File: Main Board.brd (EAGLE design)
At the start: 82.5 x 69.8 mm, 4 parts

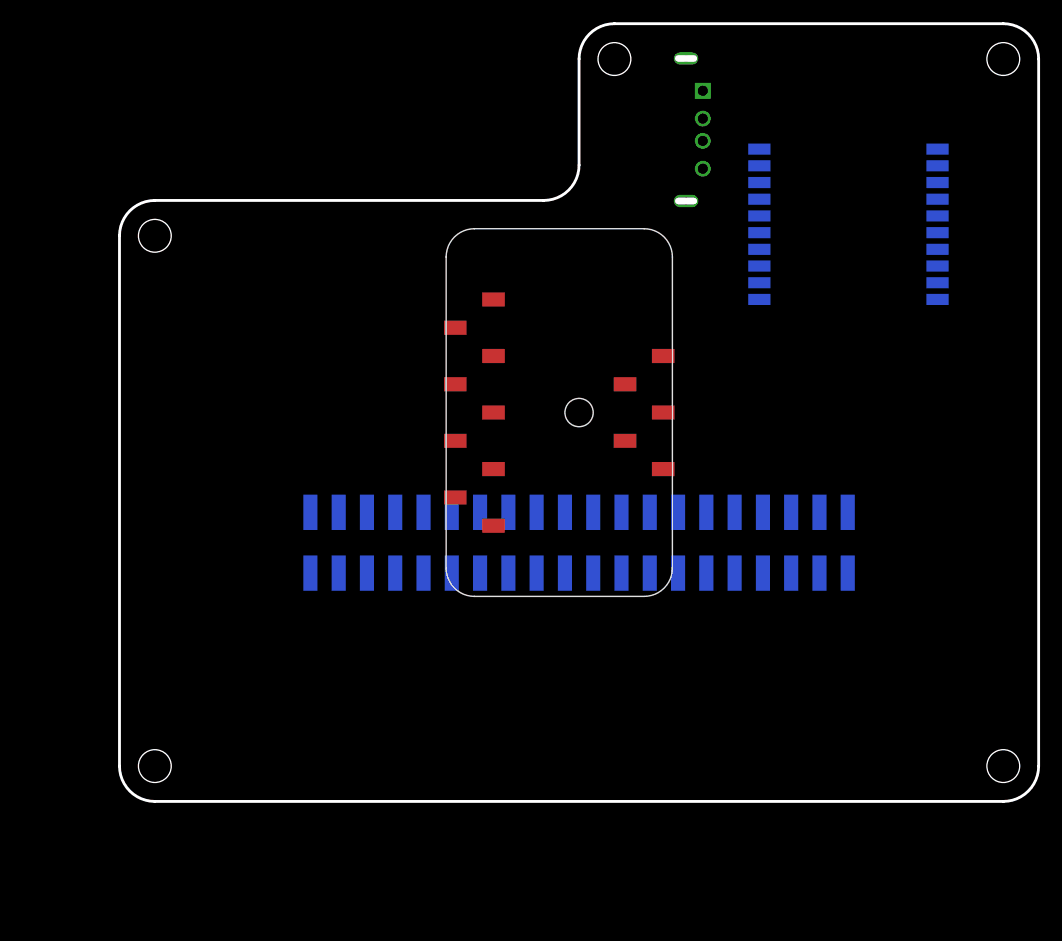
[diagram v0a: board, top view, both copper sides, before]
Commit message: Added Vishay and Bourns part libraries
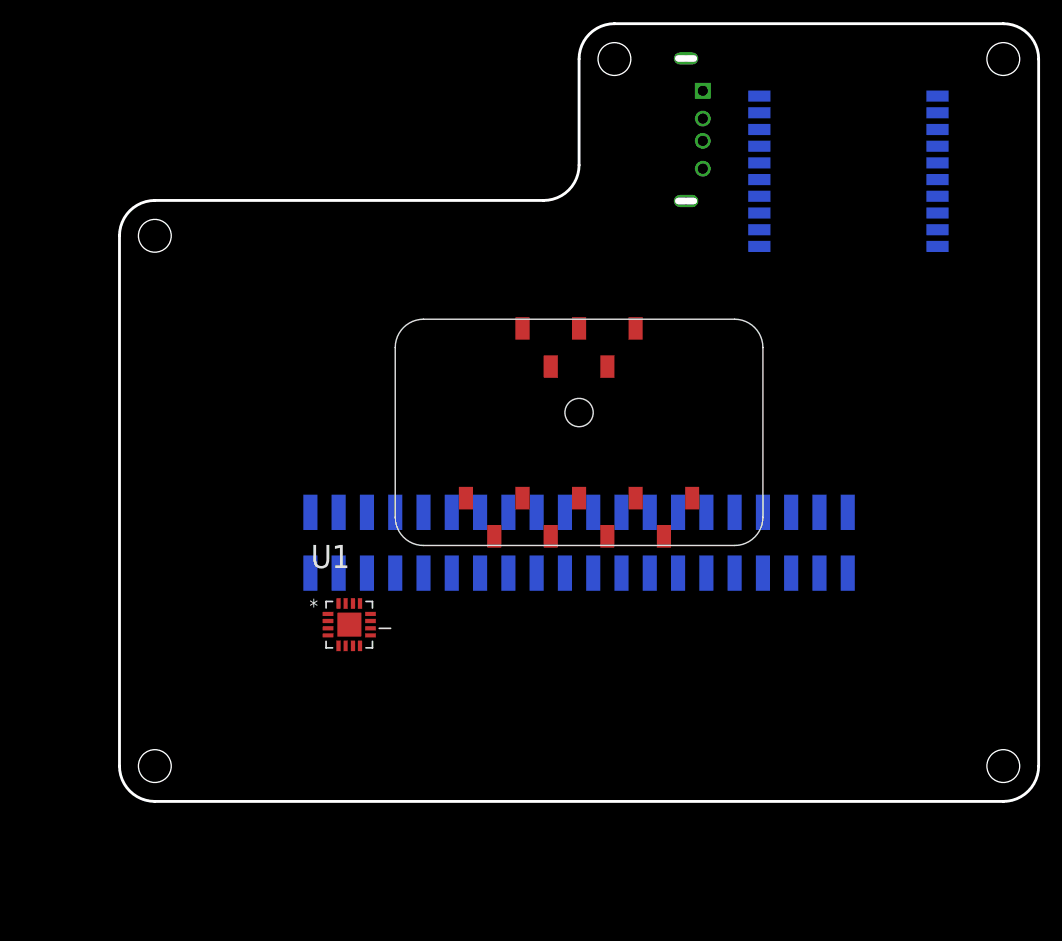
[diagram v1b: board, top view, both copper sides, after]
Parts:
- added U1: TPS61030RSAR, Texas Instruments:QFN65P400X400X100-17N
- moved U$5 4.76 mm to (23.8, 17.5)
- turned U$6 to 0 degrees
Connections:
- new net VBAT: U1.11, U1.8
- net +5V: now also U1.1, U1.15, U1.16
- net GND: now also U1.10, U1.13, U1.2, U1.5, U1.6, U1.7
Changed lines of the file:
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@@
 </autorouter>
 <elements>
-<element name="U$5" library="GoatFinder" package="GPS" value="GPS" x="23.8125" y="12.7" rot="MR180"/>
-<element name="U$6" library="GoatFinder" package="9DOF" value="9DOF" x="0" y="0" rot="R270"/>
+<element name="U$5" library="GoatFinder" package="GPS" value="GPS" x="23.8125" y="17.4625" rot="MR180"/>
+<element name="U$6" library="GoatFinder" package="9DOF" value="9DOF" x="0" y="0"/>
 <element name="U$8" library="GoatFinder" package="USB_VERTICLE" value="USB_VERTICLE" x="11.1125" y="25.4" rot="R90"/>
 <element name="U$11" library="GoatFinder" package="PI_HEADER_SMD" value="PI" x="0" y="-11.5"/>
+<element name="U1" library="Texas Instruments" package="QFN65P400X400X100-17N" value="TPS61030RSAR" x="-20.6375" y="-19.05">
+<attribute name="MPN" value="TPS61030RSAR" x="-20.6375" y="-19.05" size="1.778" layer="27" display="off"/>
+<attribute name="OC_FARNELL" value="1813710" x="-20.6375" y="-19.05" size="1.778" layer="27" display="off"/>
+<attribute name="OC_NEWARK" value="90H4859" x="-20.6375" y="-19.05" size="1.778" layer="27" display="off"/>
+<attribute name="PACKAGE" value="QFN-16" x="-20.6375" y="-19.05" size="1.778" layer="27" display="off"/>
+<attribute name="SUPPLIER" value="Texas Instruments" x="-20.6375" y="-19.05" size="1.778" layer="27" display="off"/>
+</element>
 </elements>
 <signals>
@@
 <contactref element="U$11" pad="5V@4"/>
 <contactref element="U$6" pad="P$20"/>
-<wire x1="-7.683" y1="10.16" x2="11.1125" y2="28.9" width="0" layer="19" extent="1-1"/>
-<wire x1="-21.59" y1="-14.421" x2="-7.683" y2="10.16" width="0" layer="19" extent="1-16"/>
+<contactref element="U1" pad="16"/>
+<contactref element="U1" pad="15"/>
+<contactref element="U1" pad="1"/>
+<wire x1="-10.16" y1="-7.683" x2="11.1125" y2="28.9" width="0" layer="19" extent="1-1"/>
+<wire x1="-21.59" y1="-14.421" x2="-10.16" y2="-7.683" width="0" layer="19" extent="1-16"/>
 <wire x1="-24.13" y1="-14.421" x2="-21.59" y2="-14.421" width="0" layer="19" extent="16-16"/>
+<wire x1="-21.6027" y1="-17.145" x2="-21.59" y2="-14.421" width="0" layer="19" extent="1-16"/>
+<wire x1="-20.9677" y1="-17.145" x2="-21.6027" y2="-17.145" width="0" layer="19" extent="1-1"/>
+<wire x1="-22.5425" y1="-18.0848" x2="-21.6027" y2="-17.145" width="0" layer="19" extent="1-1"/>
 </signal>
 <signal name="GND">
@@
 <contactref element="U$11" pad="GND@39"/>
 <contactref element="U$6" pad="P$22"/>
-<wire x1="32.1925" y1="11.66" x2="32.1925" y2="22.16" width="0" layer="19" extent="16-16"/>
-<wire x1="16.1925" y1="20.66" x2="32.1925" y2="22.16" width="0" layer="19" extent="16-16"/>
-<wire x1="11.1125" y1="21.9" x2="16.1925" y2="20.66" width="0" layer="19" extent="16-16"/>
+<contactref element="U1" pad="7"/>
+<contactref element="U1" pad="5"/>
+<contactref element="U1" pad="6"/>
+<contactref element="U1" pad="13"/>
+<contactref element="U1" pad="10"/>
+<contactref element="U1" pad="2"/>
+<wire x1="32.1925" y1="16.4225" x2="32.1925" y2="26.9225" width="0" layer="19" extent="16-16"/>
+<wire x1="16.1925" y1="25.4225" x2="32.1925" y2="26.9225" width="0" layer="19" extent="16-16"/>
+<wire x1="11.1125" y1="21.9" x2="16.1925" y2="25.4225" width="0" layer="19" extent="16-16"/>
 <wire x1="9.6125" y1="19" x2="11.1125" y2="21.9" width="0" layer="19" extent="1-1"/>
-<wire x1="16.1925" y1="13.16" x2="16.1925" y2="20.66" width="0" layer="19" extent="16-16"/>
+<wire x1="16.1925" y1="17.9225" x2="16.1925" y2="25.4225" width="0" layer="19" extent="16-16"/>
 <wire x1="9.6125" y1="31.8" x2="11.1125" y2="21.9" width="0" layer="19" extent="1-1"/>
-<wire x1="24.13" y1="-8.96" x2="32.1925" y2="11.66" width="0" layer="19" extent="16-16"/>
+<wire x1="24.13" y1="-8.96" x2="32.1925" y2="16.4225" width="0" layer="19" extent="16-16"/>
 <wire x1="16.51" y1="-14.421" x2="24.13" y2="-8.96" width="0" layer="19" extent="16-16"/>
 <wire x1="11.43" y1="-14.421" x2="16.51" y2="-14.421" width="0" layer="19" extent="16-16"/>
@@
 <wire x1="-13.97" y1="-8.96" x2="-8.89" y2="-14.421" width="0" layer="19" extent="16-16"/>
 <wire x1="-19.05" y1="-14.421" x2="-13.97" y2="-8.96" width="0" layer="19" extent="16-16"/>
-<wire x1="-7.683" y1="5.08" x2="-13.97" y2="-8.96" width="0" layer="19" extent="1-16"/>
+<wire x1="-19.6723" y1="-17.145" x2="-19.05" y2="-14.421" width="0" layer="19" extent="1-16"/>
+<wire x1="-18.7325" y1="-19.3802" x2="-19.6723" y2="-17.145" width="0" layer="19" extent="1-1"/>
+<wire x1="-20.3073" y1="-20.955" x2="-18.7325" y2="-19.3802" width="0" layer="19" extent="1-1"/>
+<wire x1="-20.9677" y1="-20.955" x2="-20.3073" y2="-20.955" width="0" layer="19" extent="1-1"/>
+<wire x1="-21.6027" y1="-20.955" x2="-20.9677" y2="-20.955" width="0" layer="19" extent="1-1"/>
+<wire x1="-22.5425" y1="-18.7198" x2="-21.6027" y2="-20.955" width="0" layer="19" extent="1-1"/>
+<wire x1="-5.08" y1="-7.683" x2="-1.27" y2="-14.421" width="0" layer="19" extent="1-16"/>
 </signal>
 <signal name="+3.3V">
@@
 <contactref element="U$11" pad="3.3V@17"/>
 <contactref element="U$6" pad="P$21"/>
-<wire x1="-3.81" y1="-8.96" x2="-24.13" y2="-8.96" width="0" layer="19" extent="16-16"/>
-<wire x1="-11.113" y1="7.62" x2="-3.81" y2="-8.96" width="0" layer="19" extent="1-16"/>
-<wire x1="16.1925" y1="10.16" x2="-11.113" y2="7.62" width="0" layer="19" extent="1-16"/>
+<wire x1="-7.62" y1="-11.113" x2="-24.13" y2="-8.96" width="0" layer="19" extent="1-16"/>
+<wire x1="-3.81" y1="-8.96" x2="-7.62" y2="-11.113" width="0" layer="19" extent="1-16"/>
+<wire x1="16.1925" y1="14.9225" x2="-3.81" y2="-8.96" width="0" layer="19" extent="16-16"/>
 </signal>
 <signal name="CE0">
@@
 <contactref element="U$11" pad="SCL1"/>
 <contactref element="U$6" pad="P$23"/>
-<wire x1="-11.113" y1="2.54" x2="-19.05" y2="-8.96" width="0" layer="19" extent="1-16"/>
+<wire x1="-2.54" y1="-11.113" x2="-19.05" y2="-8.96" width="0" layer="19" extent="1-16"/>
 </signal>
 <signal name="SDA1">
 <contactref element="U$11" pad="SDA1"/>
 <contactref element="U$6" pad="P$24"/>
-<wire x1="-7.683" y1="0" x2="-21.59" y2="-8.96" width="0" layer="19" extent="1-16"/>
+<wire x1="0" y1="-7.683" x2="-21.59" y2="-8.96" width="0" layer="19" extent="1-16"/>
+</signal>
+<signal name="VBAT">
+<contactref element="U1" pad="8"/>
+<contactref element="U1" pad="11"/>
+<wire x1="-18.7325" y1="-18.7198" x2="-19.6723" y2="-20.955" width="0" layer="19" extent="1-1"/>
 </signal>
 </signals>

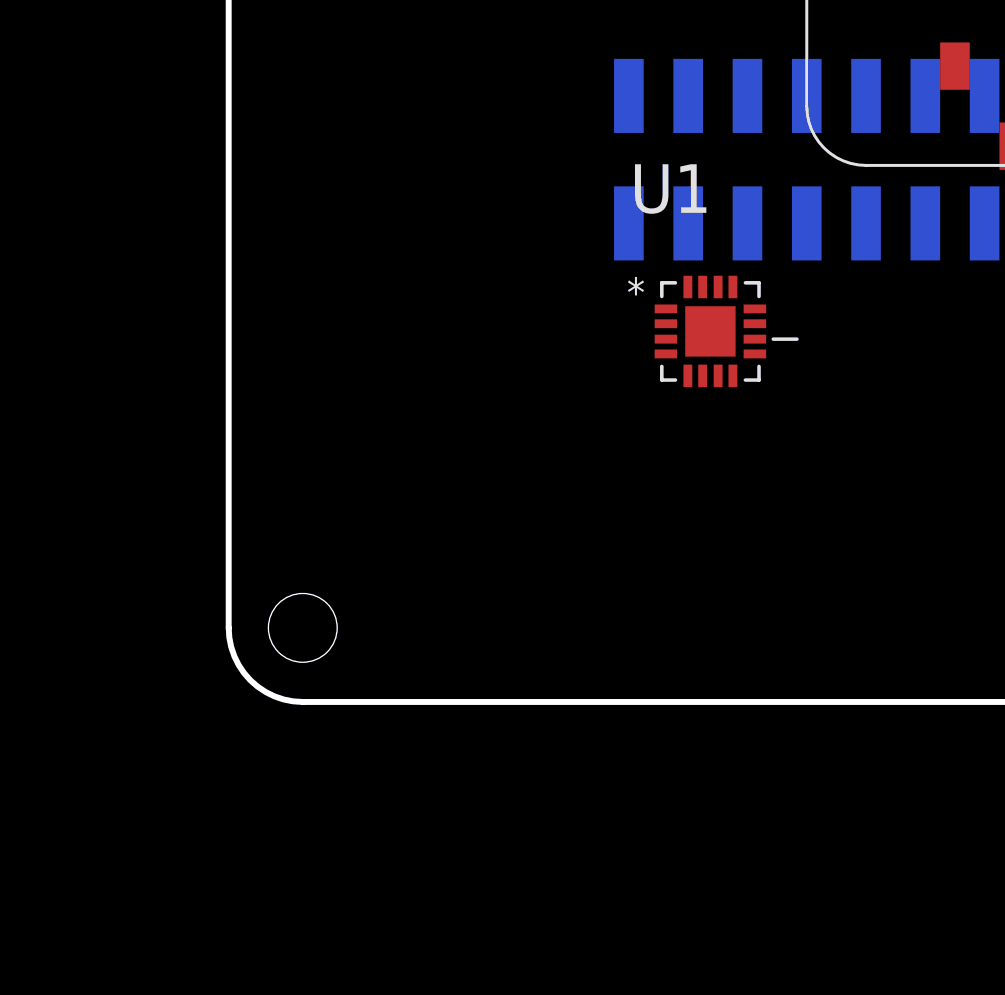
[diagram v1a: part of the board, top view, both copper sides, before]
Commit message: Finished +5V Power Supply Schematic
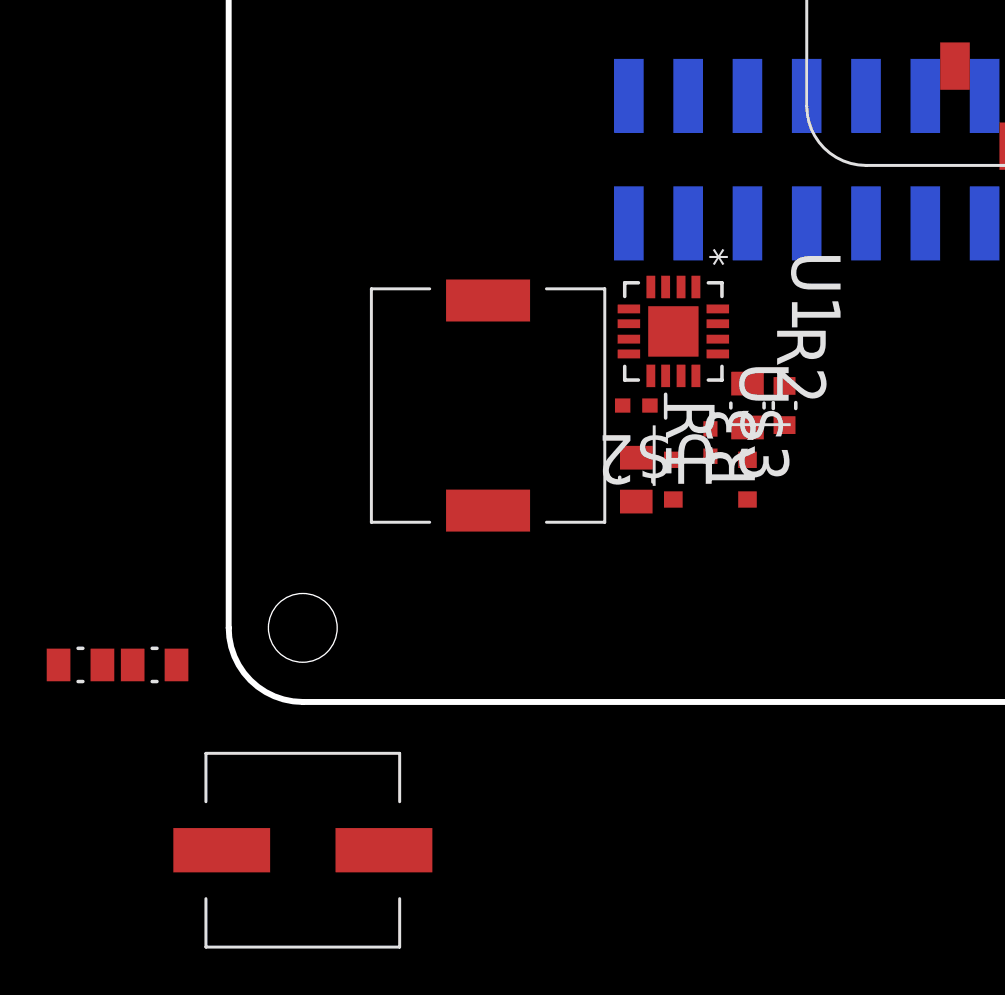
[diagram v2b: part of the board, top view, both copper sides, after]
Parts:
- added R1: 390K Ohm, Vishay:RESC2013X65N
- added R2: 182K Ohms, Vishay:RESC2013X65N
- added R3: 1.65M Ohms, Vishay:RESC1608X60N
- added U$1: 6.2uH, GoatFinder:SRU1038-6R2Y
- added U$10, U$9: 0805CAP, GoatFinder:RESC2013X45N
- added U$12: 220, GoatFinder:220
- added U$2, U$3: 2.67M, Vishay:RESC1005X40N
- added U$4: 10pF, GoatFinder:0603
- added U$7: 0603CAP, GoatFinder:0603
- moved U1 1.59 mm to (-22.2, -19.1), turned to 270 degrees
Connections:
- new net N$1: R1.1, U$2.2, U1.9
- new net N$11: R2.2, R3.2, U$4.P$1, U1.14
- new net N$2: U$1.P$1, U1.3, U1.4
- new net N$7: U$3.2, U1.12
- net +5V: now also R3.1, U$12.P$1, U$3.1, U$4.P$2, U$9.1
- net GND: now also R2.1, U$10.2, U$12.P$2, U$2.1, U$7.P$2, U$9.2
- net VBAT: now also R1.2, U$1.P$2, U$10.1, U$7.P$1

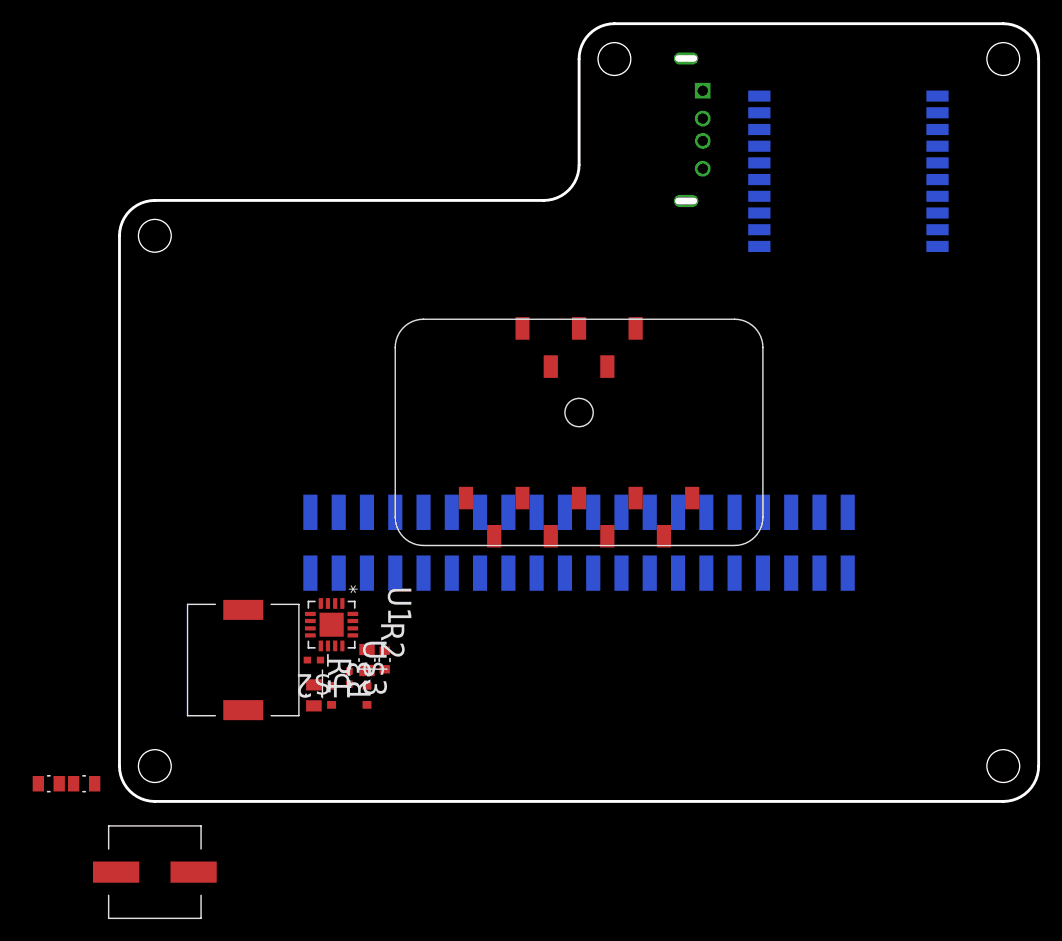
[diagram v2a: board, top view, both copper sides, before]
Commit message: Completed Barometer / Altitude Schematic
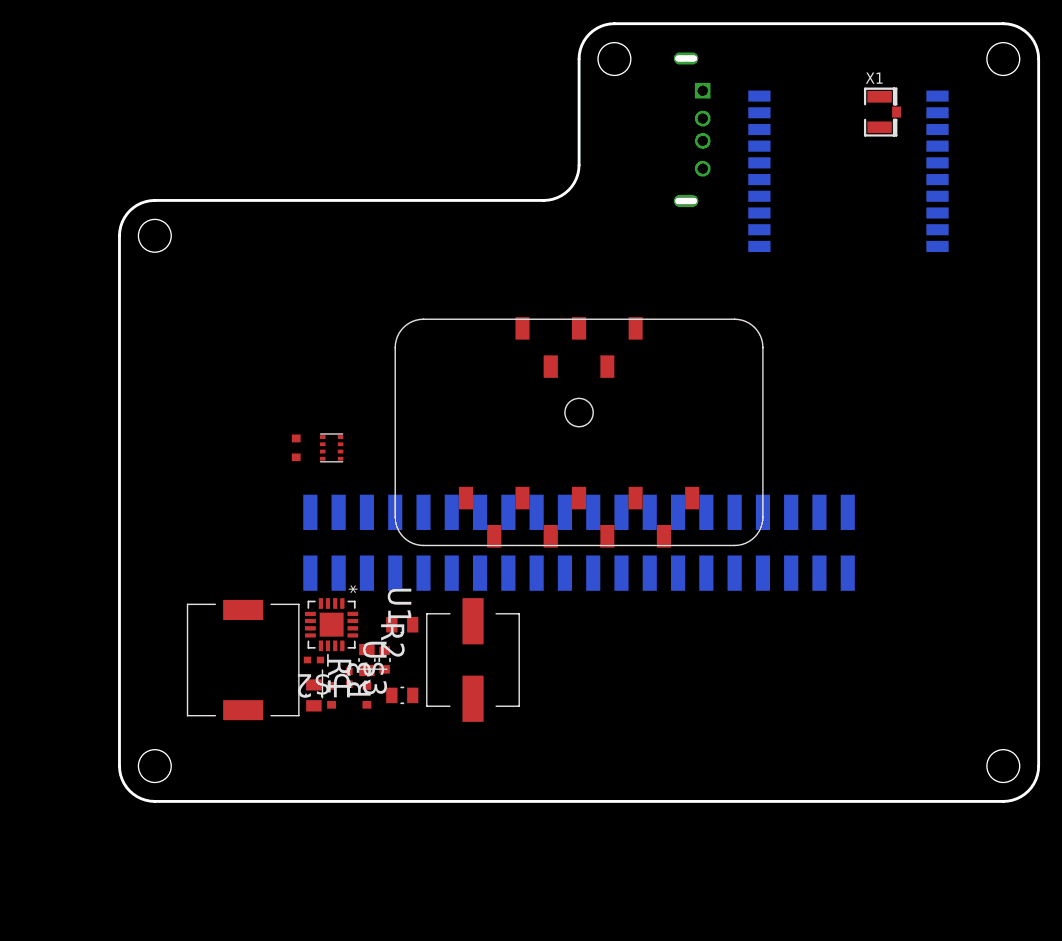
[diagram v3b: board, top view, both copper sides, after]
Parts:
- added U$13: BMP280, GoatFinder:BMP280
- added U$14: 0603CAP, GoatFinder:0603
- added X1: (no value), Adafruit:U.FL
- moved U$10 34.8 mm to (-15.9, -19.1)
- moved U$12 34.3 mm to (-9.53, -22.2), turned to 90 degrees
- moved U$9 29.7 mm to (-15.9, -25.4)
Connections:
- net SCL1 renamed N$14
- net SDA1 renamed N$13
- removed net CE0: U$11.CE0
- new net N$10: U$11.SCL0, U$13.P$4
- new net N$12: U$11.SDA0, U$13.P$3
- new net N$3: U$11.RXD, U$5.P$9
- new net N$4: U$11.TXD, U$5.P$10
- new net N$5: U$11.GPIO27, U$5.P$2
- new net N$6: U$11.GPIO28, U$5.P$5
- new net N$8: U$5.P$11, X1.3
- new net N$9: U$11.GPIO29, U$5.P$13
- net +3.3V: now also U$13.P$2, U$13.P$5, U$13.P$6, U$13.P$8, U$14.P$1
- net GND: now also U$13.P$1, U$13.P$7, U$14.P$2, X1.1, X1.2
